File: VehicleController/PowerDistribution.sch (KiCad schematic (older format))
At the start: 7 parts

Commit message: Vehicle Controller updates
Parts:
- added C3, C4: C_Small, symbol C_Small
- added U4: AP1117, TO_SOT_Packages_SMD:SOT-223, symbol AP1117
- gave numbers to parts that had none: 7
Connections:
- net GND: now also C3.2, C4.2, U4.1 (GND/ADJ)
- net PowerIn renamed PWR_IN
- net PowerOut renamed 12V
- net 12V: now also C3.1, U4.3 (VI)
- new net 5V: C4.1, U4.2 (VO), U4.4 (VO)
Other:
- moved on the sheet: D1, F1, R1, R2, R3, U2, U3

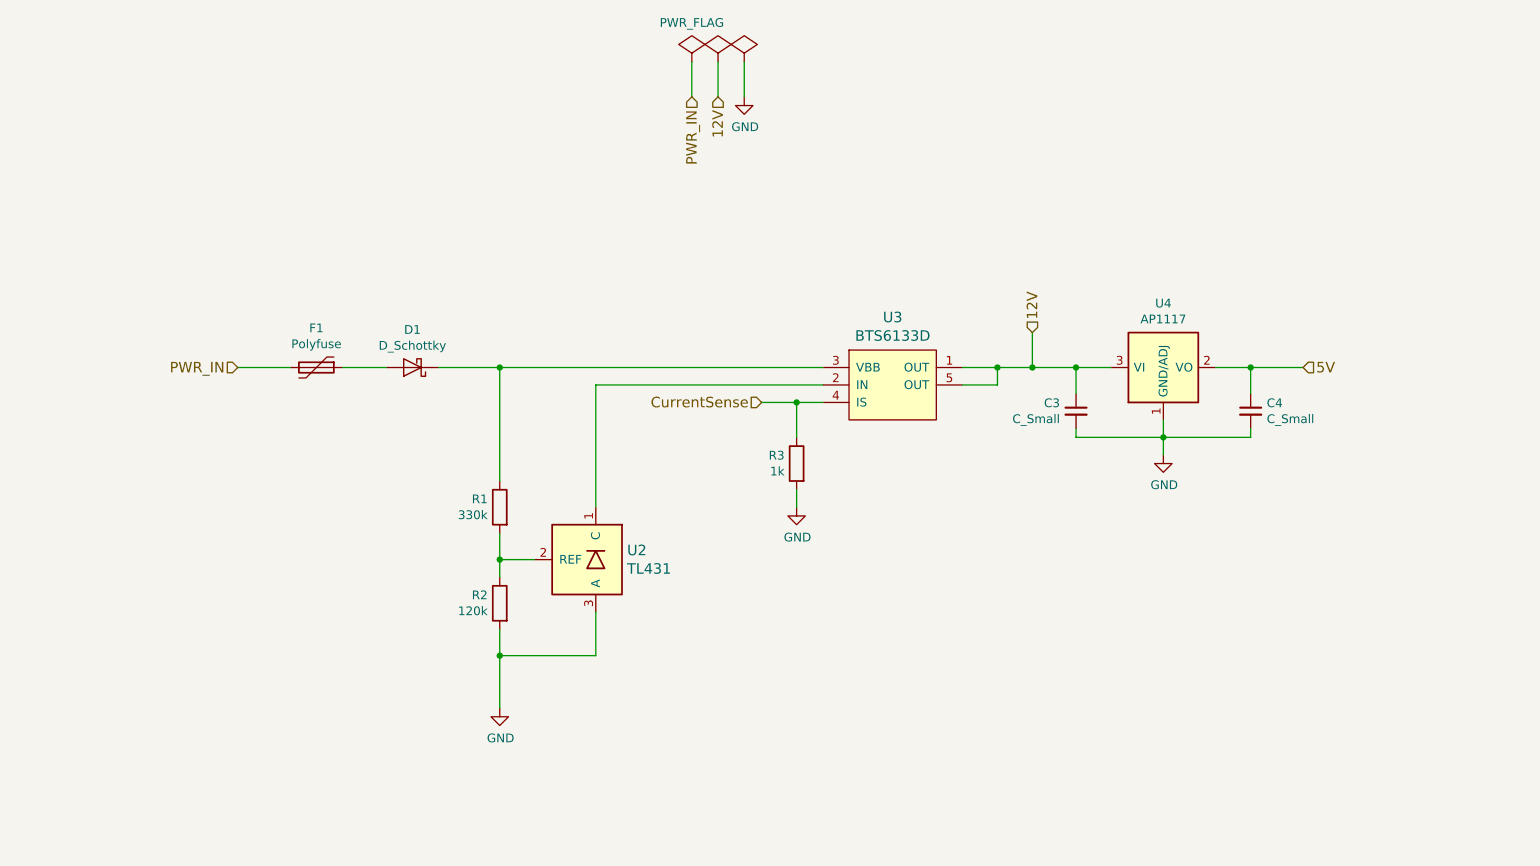
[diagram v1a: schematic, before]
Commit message: Added GPS, DAC, Isolation sheet, buzzer to VC
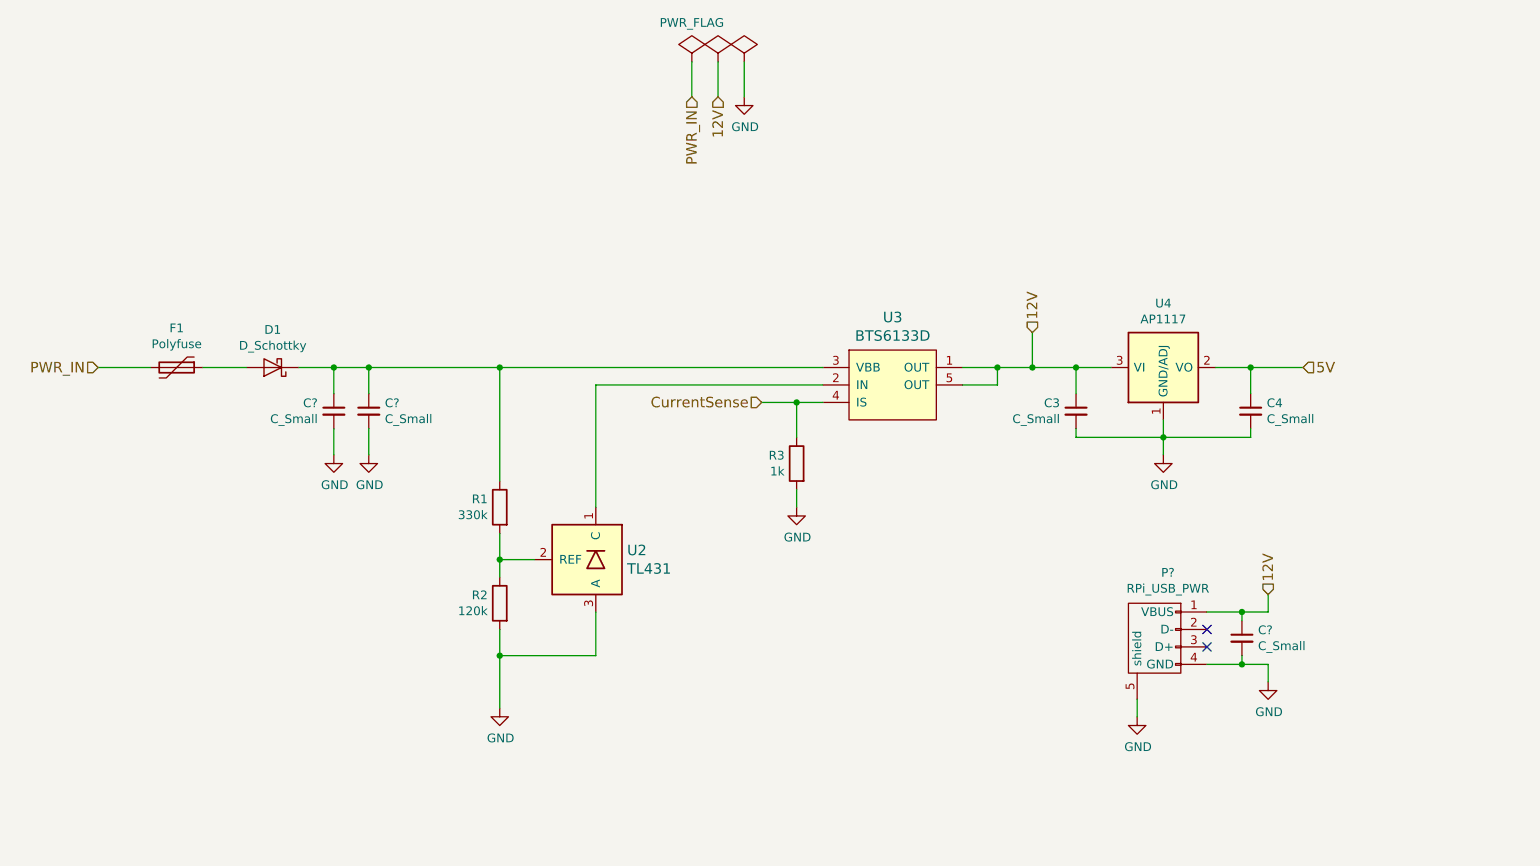
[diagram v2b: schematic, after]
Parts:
- added C? (x3): C_Small, symbol C_Small
- added P?: RPi_USB_PWR, symbol USB_A
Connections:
- net 12V: now also C?.1, P?.1 (VBUS)
- net GND: now also C?.2, C?.2, C?.2, P?.4 (GND), P?.5 (shield)
- net at D1.1 (K), R1.1, U3.3 (VBB): now also C?.1, C?.1
- no-connect marks 0 -> 2
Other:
- moved on the sheet: D1, F1
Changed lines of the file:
@@
 $Descr A4 11693 8268
 encoding utf-8
-Sheet 2 4
+Sheet 2 5
 Title ""
 Date ""
@@
 L D_Schottky D1
 U 1 1 587C7BB2
-P 3800 2750
-F 0 "D1" H 3800 2534 50  0000 C CNN
-F 1 "D_Schottky" H 3800 2625 50  0000 C CNN
-F 2 "" H 3800 2750 50  0000 C CNN
-F 3 "" H 3800 2750 50  0000 C CNN
-	1    3800 2750
+P 3000 2750
+F 0 "D1" H 3000 2534 50  0000 C CNN
+F 1 "D_Schottky" H 3000 2625 50  0000 C CNN
+F 2 "" H 3000 2750 50  0000 C CNN
+F 3 "" H 3000 2750 50  0000 C CNN
+	1    3000 2750
 	-1   0    0    1
 $EndComp
@@
 L Polyfuse F1
 U 1 1 587C7BB9
-P 3250 2750
-F 0 "F1" V 3025 2750 50  0000 C CNN
-F 1 "Polyfuse" V 3116 2750 50  0000 C CNN
-F 2 "" H 3300 2550 50  0001 L CNN
-F 3 "" H 3250 2750 50  0001 C CNN
-	1    3250 2750
+P 2450 2750
+F 0 "F1" V 2225 2750 50  0000 C CNN
+F 1 "Polyfuse" V 2316 2750 50  0000 C CNN
+F 2 "" H 2500 2550 50  0001 L CNN
+F 3 "" H 2450 2750 50  0001 C CNN
+	1    2450 2750
 	0    1    1    0
 $EndComp
@@
 	4850 2850 6150 2850
 Wire Wire Line
-	3950 2750 6150 2750
+	3150 2750 6150 2750
 Wire Wire Line
 	4300 2750 4300 3400
@@
 Connection ~ 4300 3850
 Wire Wire Line
-	3400 2750 3650 2750
-Wire Wire Line
-	2800 2750 3100 2750
+	2600 2750 2850 2750
+Wire Wire Line
+	2000 2750 2300 2750
 $Comp
 L GND #PWR015
@@
 	7150 2850 7150 2750
 Connection ~ 7150 2750
-Text HLabel 2800 2750 0    60   Input ~ 0
+Text HLabel 2000 2750 0    60   Input ~ 0
 PWR_IN
 Text HLabel 5800 2950 0    60   Input ~ 0
@@
 Wire Wire Line
 	5400 1200 5400 1000
+$Comp
+L USB_A P?
+U 1 1 58B30D8B
+P 8050 4350
+F 0 "P?" V 7625 4274 50  0000 C CNN
+F 1 "RPi_USB_PWR" V 7716 4274 50  0000 C CNN
+F 2 "" V 8000 4250 50  0000 C CNN
+F 3 "" V 8000 4250 50  0000 C CNN
+	1    8050 4350
+	0    -1   1    0
+$EndComp
+$Comp
+L C_Small C?
+U 1 1 58B30D92
+P 8550 4300
+F 0 "C?" H 8642 4346 50  0000 L CNN
+F 1 "C_Small" H 8642 4255 50  0000 L CNN
+F 2 "" H 8550 4300 50  0000 C CNN
+F 3 "" H 8550 4300 50  0000 C CNN
+	1    8550 4300
+	1    0    0    -1
+$EndComp
+$Comp
+L GND #PWR?
+U 1 1 58B30D9F
+P 7950 4750
+F 0 "#PWR?" H 7950 4500 50  0001 C CNN
+F 1 "GND" H 7955 4577 50  0000 C CNN
+F 2 "" H 7950 4750 50  0000 C CNN
+F 3 "" H 7950 4750 50  0000 C CNN
+	1    7950 4750
+	1    0    0    -1
+$EndComp
+NoConn ~ 8350 4250
+NoConn ~ 8350 4350
+Connection ~ 8550 4150
+Wire Wire Line
+	8550 4200 8550 4150
+Connection ~ 8550 4450
+Wire Wire Line
+	8550 4400 8550 4450
+Wire Wire Line
+	8700 4450 8700 4550
+Wire Wire Line
+	8350 4450 8700 4450
+Wire Wire Line
+	7950 4750 7950 4650
+Wire Wire Line
+	8700 4150 8700 4050
+Wire Wire Line
+	8350 4150 8700 4150
+Text HLabel 8700 4050 1    60   Input ~ 0
+12V
+$Comp
+L GND #PWR?
+U 1 1 58B31164
+P 8700 4550
+F 0 "#PWR?" H 8700 4300 50  0001 C CNN
+F 1 "GND" H 8705 4377 50  0000 C CNN
+F 2 "" H 8700 4550 50  0000 C CNN
+F 3 "" H 8700 4550 50  0000 C CNN
+	1    8700 4550
+	1    0    0    -1
+$EndComp
+$Comp
+L C_Small C?
+U 1 1 58B0EE62
+P 3350 3000
+F 0 "C?" H 3442 3046 50  0000 L CNN
+F 1 "C_Small" H 3442 2955 50  0000 L CNN
+F 2 "" H 3350 3000 50  0000 C CNN
+F 3 "" H 3350 3000 50  0000 C CNN
+	1    3350 3000
+	-1   0    0    -1
+$EndComp
+$Comp
+L C_Small C?
+U 1 1 58B0EEFF
+P 3550 3000
+F 0 "C?" H 3642 3046 50  0000 L CNN
+F 1 "C_Small" H 3642 2955 50  0000 L CNN
+F 2 "" H 3550 3000 50  0000 C CNN
+F 3 "" H 3550 3000 50  0000 C CNN
+	1    3550 3000
+	1    0    0    -1
+$EndComp
+Wire Wire Line
+	3350 2900 3350 2750
+Connection ~ 3350 2750
+Wire Wire Line
+	3550 2900 3550 2750
+Connection ~ 3550 2750
+$Comp
+L GND #PWR?
+U 1 1 58B0EFE3
+P 3350 3250
+F 0 "#PWR?" H 3350 3000 50  0001 C CNN
+F 1 "GND" H 3355 3077 50  0000 C CNN
+F 2 "" H 3350 3250 50  0000 C CNN
+F 3 "" H 3350 3250 50  0000 C CNN
+	1    3350 3250
+	1    0    0    -1
+$EndComp
+Wire Wire Line
+	3350 3250 3350 3100
+Wire Wire Line
+	3550 3250 3550 3100
+$Comp
+L GND #PWR?
+U 1 1 58B0F09D
+P 3550 3250
+F 0 "#PWR?" H 3550 3000 50  0001 C CNN
+F 1 "GND" H 3555 3077 50  0000 C CNN
+F 2 "" H 3550 3250 50  0000 C CNN
+F 3 "" H 3550 3250 50  0000 C CNN
+	1    3550 3250
+	1    0    0    -1
+$EndComp
 $EndSCHEMATC

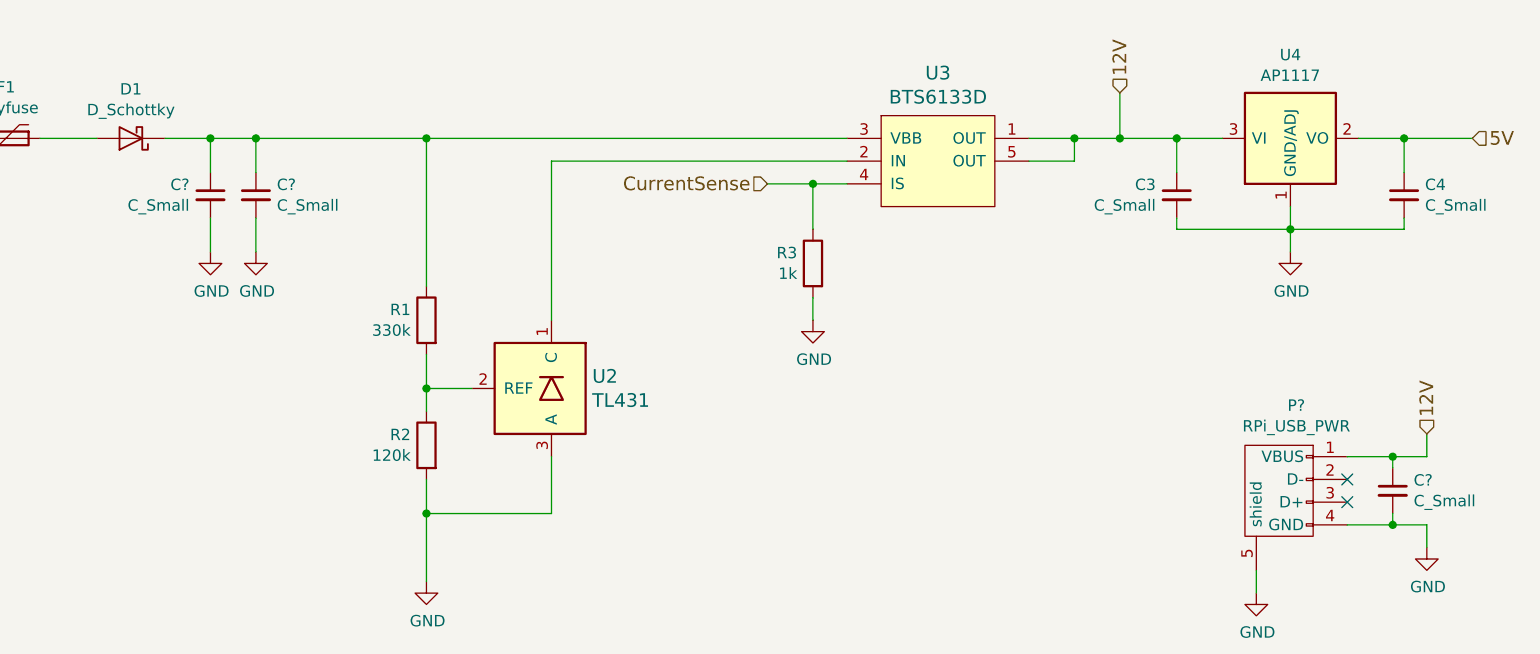
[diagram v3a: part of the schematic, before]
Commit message: Add High-G Accel, connectors
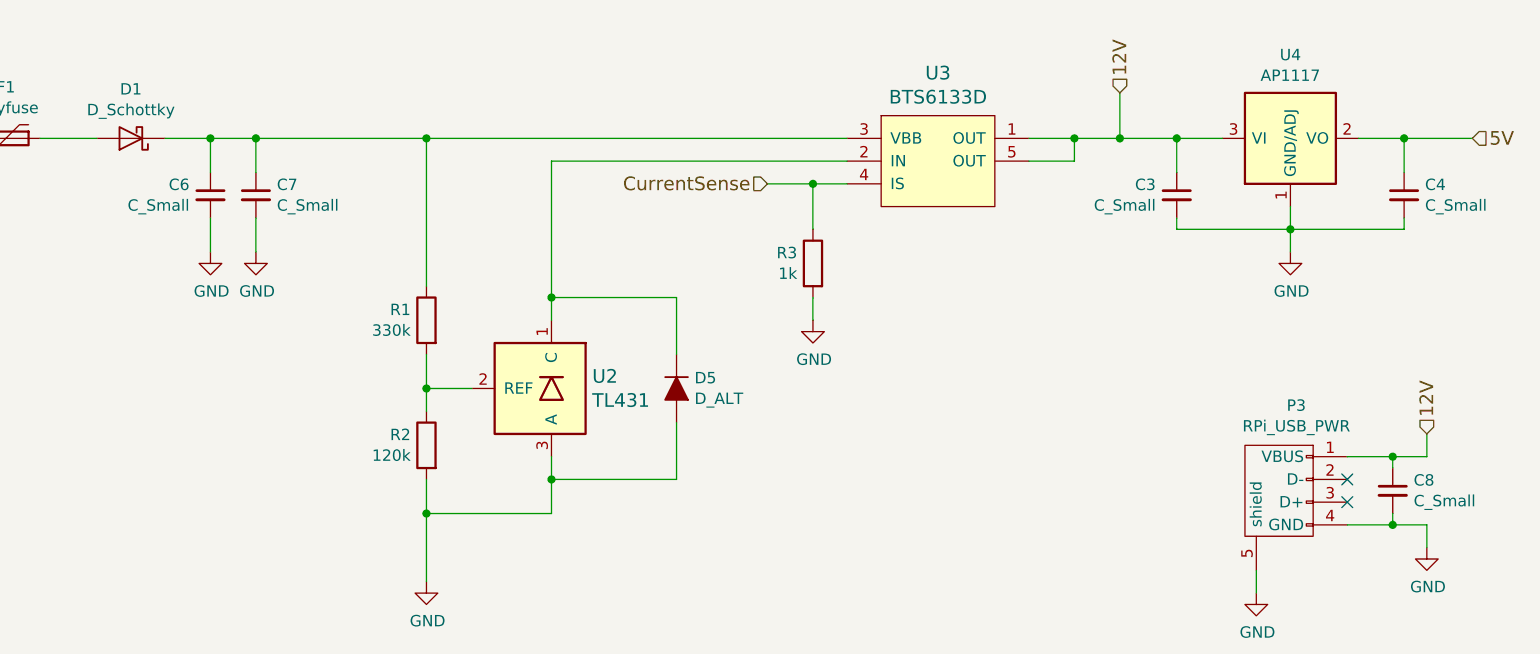
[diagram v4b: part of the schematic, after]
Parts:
- added D5: D_ALT, symbol D_ALT
- gave numbers to parts that had none: 4
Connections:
- net GND: now also D5.2 (A)
- net at U2.1 (C), U3.2 (IN): now also D5.1 (K)
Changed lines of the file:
@@
 LIBS:dc-dc
 LIBS:Power_Management
+LIBS:switches
 LIBS:VehicleController-cache
 EELAYER 26 0
@@
 $EndComp
 $Comp
-L GND #PWR014
+L GND #PWR26
 U 1 1 587C7BE3
 P 6000 3550
-F 0 "#PWR014" H 6000 3300 50  0001 C CNN
+F 0 "#PWR26" H 6000 3300 50  0001 C CNN
 F 1 "GND" H 6005 3377 50  0000 C CNN
 F 2 "" H 6000 3550 50  0000 C CNN
@@
 	1    0    0    -1
 $EndComp
-Wire Wire Line
-	6000 3150 6000 2950
-Wire Wire Line
-	5800 2950 6150 2950
-Wire Wire Line
-	4850 3550 4850 2850
-Wire Wire Line
-	4850 2850 6150 2850
-Wire Wire Line
-	3150 2750 6150 2750
-Wire Wire Line
-	4300 2750 4300 3400
-Connection ~ 4300 2750
-Wire Wire Line
-	6000 3550 6000 3450
-Wire Wire Line
-	4300 3700 4300 3950
-Wire Wire Line
-	4500 3850 4300 3850
-Connection ~ 4300 3850
-Wire Wire Line
-	2600 2750 2850 2750
-Wire Wire Line
-	2000 2750 2300 2750
-$Comp
-L GND #PWR015
+$Comp
+L GND #PWR24
 U 1 1 587C7BF7
 P 4300 4700
-F 0 "#PWR015" H 4300 4450 50  0001 C CNN
+F 0 "#PWR24" H 4300 4450 50  0001 C CNN
 F 1 "GND" H 4305 4527 50  0000 C CNN
 F 2 "" H 4300 4700 50  0000 C CNN
@@
 	1    0    0    -1
 $EndComp
-Wire Wire Line
-	4300 4250 4300 4700
-Wire Wire Line
-	4300 4400 4850 4400
-Wire Wire Line
-	4850 4400 4850 4150
-Connection ~ 4300 4400
-Wire Wire Line
-	6950 2850 7150 2850
-Wire Wire Line
-	7150 2850 7150 2750
-Connection ~ 7150 2750
 Text HLabel 2000 2750 0    60   Input ~ 0
 PWR_IN
 Text HLabel 5800 2950 0    60   Input ~ 0
 CurrentSense
-Connection ~ 6000 2950
 $Comp
 L AP1117 U4
@@
 $EndComp
 $Comp
-L GND #PWR016
+L GND #PWR28
 U 1 1 58AEB860
 P 8100 3250
-F 0 "#PWR016" H 8100 3000 50  0001 C CNN
+F 0 "#PWR28" H 8100 3000 50  0001 C CNN
 F 1 "GND" H 8105 3077 50  0000 C CNN
 F 2 "" H 8100 3250 50  0000 C CNN
@@
 	1    0    0    -1
 $EndComp
-Wire Wire Line
-	8100 3050 8100 3250
-Wire Wire Line
-	7600 3100 7600 3150
-Wire Wire Line
-	7600 3150 8600 3150
-Connection ~ 8100 3150
-Wire Wire Line
-	8600 3150 8600 3100
-Wire Wire Line
-	7600 2750 7600 2900
-Wire Wire Line
-	6950 2750 7800 2750
-Wire Wire Line
-	8600 2900 8600 2750
-Wire Wire Line
-	8400 2750 8900 2750
-Connection ~ 7600 2750
-Connection ~ 8600 2750
 Text HLabel 7350 2550 1    60   Input ~ 0
 12V
-Wire Wire Line
-	7350 2550 7350 2750
-Connection ~ 7350 2750
 Text HLabel 8900 2750 2    60   Input ~ 0
 5V
 $Comp
-L PWR_FLAG #FLG017
+L PWR_FLAG #FLG2
 U 1 1 58AF2028
 P 5550 1000
-F 0 "#FLG017" H 5550 1095 50  0001 C CNN
+F 0 "#FLG2" H 5550 1095 50  0001 C CNN
 F 1 "PWR_FLAG" H 5550 1224 50  0001 C CNN
 F 2 "" H 5550 1000 50  0000 C CNN
@@
 Text HLabel 5550 1200 3    60   Input ~ 0
 12V
-Wire Wire Line
-	5550 1200 5550 1000
-$Comp
-L PWR_FLAG #FLG018
+$Comp
+L PWR_FLAG #FLG3
 U 1 1 58AF2853
 P 5700 1000
-F 0 "#FLG018" H 5700 1095 50  0001 C CNN
+F 0 "#FLG3" H 5700 1095 50  0001 C CNN
 F 1 "PWR_FLAG" H 5700 1224 50  0001 C CNN
 F 2 "" H 5700 1000 50  0000 C CNN
@@
 $EndComp
 $Comp
-L GND #PWR019
+L GND #PWR25
 U 1 1 58AF29E4
 P 5700 1200
-F 0 "#PWR019" H 5700 950 50  0001 C CNN
+F 0 "#PWR25" H 5700 950 50  0001 C CNN
 F 1 "GND" H 5705 1027 50  0000 C CNN
 F 2 "" H 5700 1200 50  0000 C CNN
@@
 	1    0    0    -1
 $EndComp
-Wire Wire Line
-	5700 1200 5700 1000
 Text HLabel 5400 1200 3    60   Input ~ 0
 PWR_IN
 $Comp
-L PWR_FLAG #FLG020
+L PWR_FLAG #FLG1
 U 1 1 58AF2E1D
 P 5400 1000
-F 0 "#FLG020" H 5400 1095 50  0001 C CNN
+F 0 "#FLG1" H 5400 1095 50  0001 C CNN
 F 1 "PWR_FLAG" H 5400 1224 50  0000 C CNN
 F 2 "" H 5400 1000 50  0000 C CNN
@@
 	1    0    0    -1
 $EndComp
-Wire Wire Line
-	5400 1200 5400 1000
-$Comp
-L USB_A P?
+$Comp
+L USB_A P3
 U 1 1 58B30D8B
 P 8050 4350
-F 0 "P?" V 7625 4274 50  0000 C CNN
+F 0 "P3" V 7625 4274 50  0000 C CNN
 F 1 "RPi_USB_PWR" V 7716 4274 50  0000 C CNN
 F 2 "" V 8000 4250 50  0000 C CNN
@@
 $EndComp
 $Comp
-L C_Small C?
+L C_Small C8
 U 1 1 58B30D92
 P 8550 4300
-F 0 "C?" H 8642 4346 50  0000 L CNN
+F 0 "C8" H 8642 4346 50  0000 L CNN
 F 1 "C_Small" H 8642 4255 50  0000 L CNN
 F 2 "" H 8550 4300 50  0000 C CNN
@@
 $EndComp
 $Comp
-L GND #PWR?
+L GND #PWR27
 U 1 1 58B30D9F
 P 7950 4750
-F 0 "#PWR?" H 7950 4500 50  0001 C CNN
+F 0 "#PWR27" H 7950 4500 50  0001 C CNN
 F 1 "GND" H 7955 4577 50  0000 C CNN
 F 2 "" H 7950 4750 50  0000 C CNN
@@
 NoConn ~ 8350 4250
 NoConn ~ 8350 4350
-Connection ~ 8550 4150
-Wire Wire Line
-	8550 4200 8550 4150
-Connection ~ 8550 4450
-Wire Wire Line
-	8550 4400 8550 4450
-Wire Wire Line
-	8700 4450 8700 4550
-Wire Wire Line
-	8350 4450 8700 4450
-Wire Wire Line
-	7950 4750 7950 4650
-Wire Wire Line
-	8700 4150 8700 4050
-Wire Wire Line
-	8350 4150 8700 4150
 Text HLabel 8700 4050 1    60   Input ~ 0
 12V
 $Comp
-L GND #PWR?
+L GND #PWR29
 U 1 1 58B31164
 P 8700 4550
-F 0 "#PWR?" H 8700 4300 50  0001 C CNN
+F 0 "#PWR29" H 8700 4300 50  0001 C CNN
 F 1 "GND" H 8705 4377 50  0000 C CNN
 F 2 "" H 8700 4550 50  0000 C CNN
@@
 $EndComp
 $Comp
-L C_Small C?
+L C_Small C6
 U 1 1 58B0EE62
 P 3350 3000
-F 0 "C?" H 3442 3046 50  0000 L CNN
+F 0 "C6" H 3442 3046 50  0000 L CNN
 F 1 "C_Small" H 3442 2955 50  0000 L CNN
 F 2 "" H 3350 3000 50  0000 C CNN
@@
 $EndComp
 $Comp
-L C_Small C?
+L C_Small C7
 U 1 1 58B0EEFF
 P 3550 3000
-F 0 "C?" H 3642 3046 50  0000 L CNN
+F 0 "C7" H 3642 3046 50  0000 L CNN
 F 1 "C_Small" H 3642 2955 50  0000 L CNN
 F 2 "" H 3550 3000 50  0000 C CNN
@@
 	1    0    0    -1
 $EndComp
-Wire Wire Line
-	3350 2900 3350 2750
-Connection ~ 3350 2750
-Wire Wire Line
-	3550 2900 3550 2750
-Connection ~ 3550 2750
-$Comp
-L GND #PWR?
+$Comp
+L GND #PWR22
 U 1 1 58B0EFE3
 P 3350 3250
-F 0 "#PWR?" H 3350 3000 50  0001 C CNN
+F 0 "#PWR22" H 3350 3000 50  0001 C CNN
 F 1 "GND" H 3355 3077 50  0000 C CNN
 F 2 "" H 3350 3250 50  0000 C CNN
@@
 	1    0    0    -1
 $EndComp
-Wire Wire Line
-	3350 3250 3350 3100
-Wire Wire Line
-	3550 3250 3550 3100
-$Comp
-L GND #PWR?
+$Comp
+L GND #PWR23
 U 1 1 58B0F09D
 P 3550 3250
-F 0 "#PWR?" H 3550 3000 50  0001 C CNN
+F 0 "#PWR23" H 3550 3000 50  0001 C CNN
 F 1 "GND" H 3555 3077 50  0000 C CNN
 F 2 "" H 3550 3250 50  0000 C CNN
@@
 	1    0    0    -1
 $EndComp
+$Comp
+L D_ALT D5
+U 1 1 58B90308
+P 5400 3850
+F 0 "D5" V 5354 3929 50  0000 L CNN
+F 1 "D_ALT" V 5445 3929 50  0000 L CNN
+F 2 "" H 5400 3850 50  0000 C CNN
+F 3 "" H 5400 3850 50  0000 C CNN
+	1    5400 3850
+	0    1    1    0
+$EndComp
+Wire Wire Line
+	6000 3150 6000 2950
+Wire Wire Line
+	5800 2950 6150 2950
+Wire Wire Line
+	4850 2850 6150 2850
+Wire Wire Line
+	3150 2750 6150 2750
+Wire Wire Line
+	4300 2750 4300 3400
+Connection ~ 4300 2750
+Wire Wire Line
+	6000 3550 6000 3450
+Wire Wire Line
+	4300 3700 4300 3950
+Wire Wire Line
+	4500 3850 4300 3850
+Connection ~ 4300 3850
+Wire Wire Line
+	2600 2750 2850 2750
+Wire Wire Line
+	2000 2750 2300 2750
+Wire Wire Line
+	4300 4250 4300 4700
+Wire Wire Line
+	4300 4400 4850 4400
+Wire Wire Line
+	4850 4400 4850 4150
+Connection ~ 4300 4400
+Wire Wire Line
+	6950 2850 7150 2850
+Wire Wire Line
+	7150 2850 7150 2750
+Connection ~ 7150 2750
+Connection ~ 6000 2950
+Wire Wire Line
+	8100 3050 8100 3250
+Wire Wire Line
+	7600 3100 7600 3150
+Wire Wire Line
+	7600 3150 8600 3150
+Connection ~ 8100 3150
+Wire Wire Line
+	8600 3150 8600 3100
+Wire Wire Line
+	7600 2750 7600 2900
+Wire Wire Line
+	6950 2750 7800 2750
+Wire Wire Line
+	8600 2900 8600 2750
+Wire Wire Line
+	8400 2750 8900 2750
+Connection ~ 7600 2750
+Connection ~ 8600 2750
+Wire Wire Line
+	7350 2550 7350 2750
+Connection ~ 7350 2750
+Wire Wire Line
+	5550 1200 5550 1000
+Wire Wire Line
+	5700 1200 5700 1000
+Wire Wire Line
+	5400 1200 5400 1000
+Connection ~ 8550 4150
+Wire Wire Line
+	8550 4200 8550 4150
+Connection ~ 8550 4450
+Wire Wire Line
+	8550 4400 8550 4450
+Wire Wire Line
+	8700 4450 8700 4550
+Wire Wire Line
+	8350 4450 8700 4450
+Wire Wire Line
+	7950 4750 7950 4650
+Wire Wire Line
+	8700 4150 8700 4050
+Wire Wire Line
+	8350 4150 8700 4150
+Wire Wire Line
+	3350 2900 3350 2750
+Connection ~ 3350 2750
+Wire Wire Line
+	3550 2900 3550 2750
+Connection ~ 3550 2750
+Wire Wire Line
+	3350 3250 3350 3100
+Wire Wire Line
+	3550 3250 3550 3100
+Wire Wire Line
+	5400 3700 5400 3450
+Wire Wire Line
+	5400 3450 4850 3450
+Connection ~ 4850 3450
+Wire Wire Line
+	5400 4000 5400 4250
+Wire Wire Line
+	5400 4250 4850 4250
+Connection ~ 4850 4250
+Wire Wire Line
+	4850 2850 4850 3550
 $EndSCHEMATC
